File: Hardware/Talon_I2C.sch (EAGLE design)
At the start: 81 parts, among them J1 CONN_TALON_REMOTE, J2 CONN_I2C_LOGGER, J3 CONN_I2C_LOGGER, J4 CONN_I2C_LOGGER, J5 CONN_I2C_LOGGER, Q1 2N7002, Q2 2N7002, Q3 2N7002, Q4 2N7002, Q5 AO3419, Q6 AO3419, Q7 AO3419, Q8 AO3419, U1 SN74HC04, U10 74HC4852, U11 SN74AUP1T157DCK, U12 MCP3421A3, U13 FXMAR2102UMLP, U14 PCA9617WSON, U15 PCA9617WSON, U16 PCA9617WSON, U17 PCA9617WSON, U18 SN74AUP1G08DCK, U19 SN74AUP1G08DCK, U2 CD4044, U20 SN74AUP1G08DCK, U21 SN74AUP1G08DCK, U3 SIP32431TDFN, U4 INA4180A2, U5 MAX9034TSSOP, U6 SN74AC08, U7 24AA02SOT23, U8 MCP23018QFN, U9 PCA9536DFN

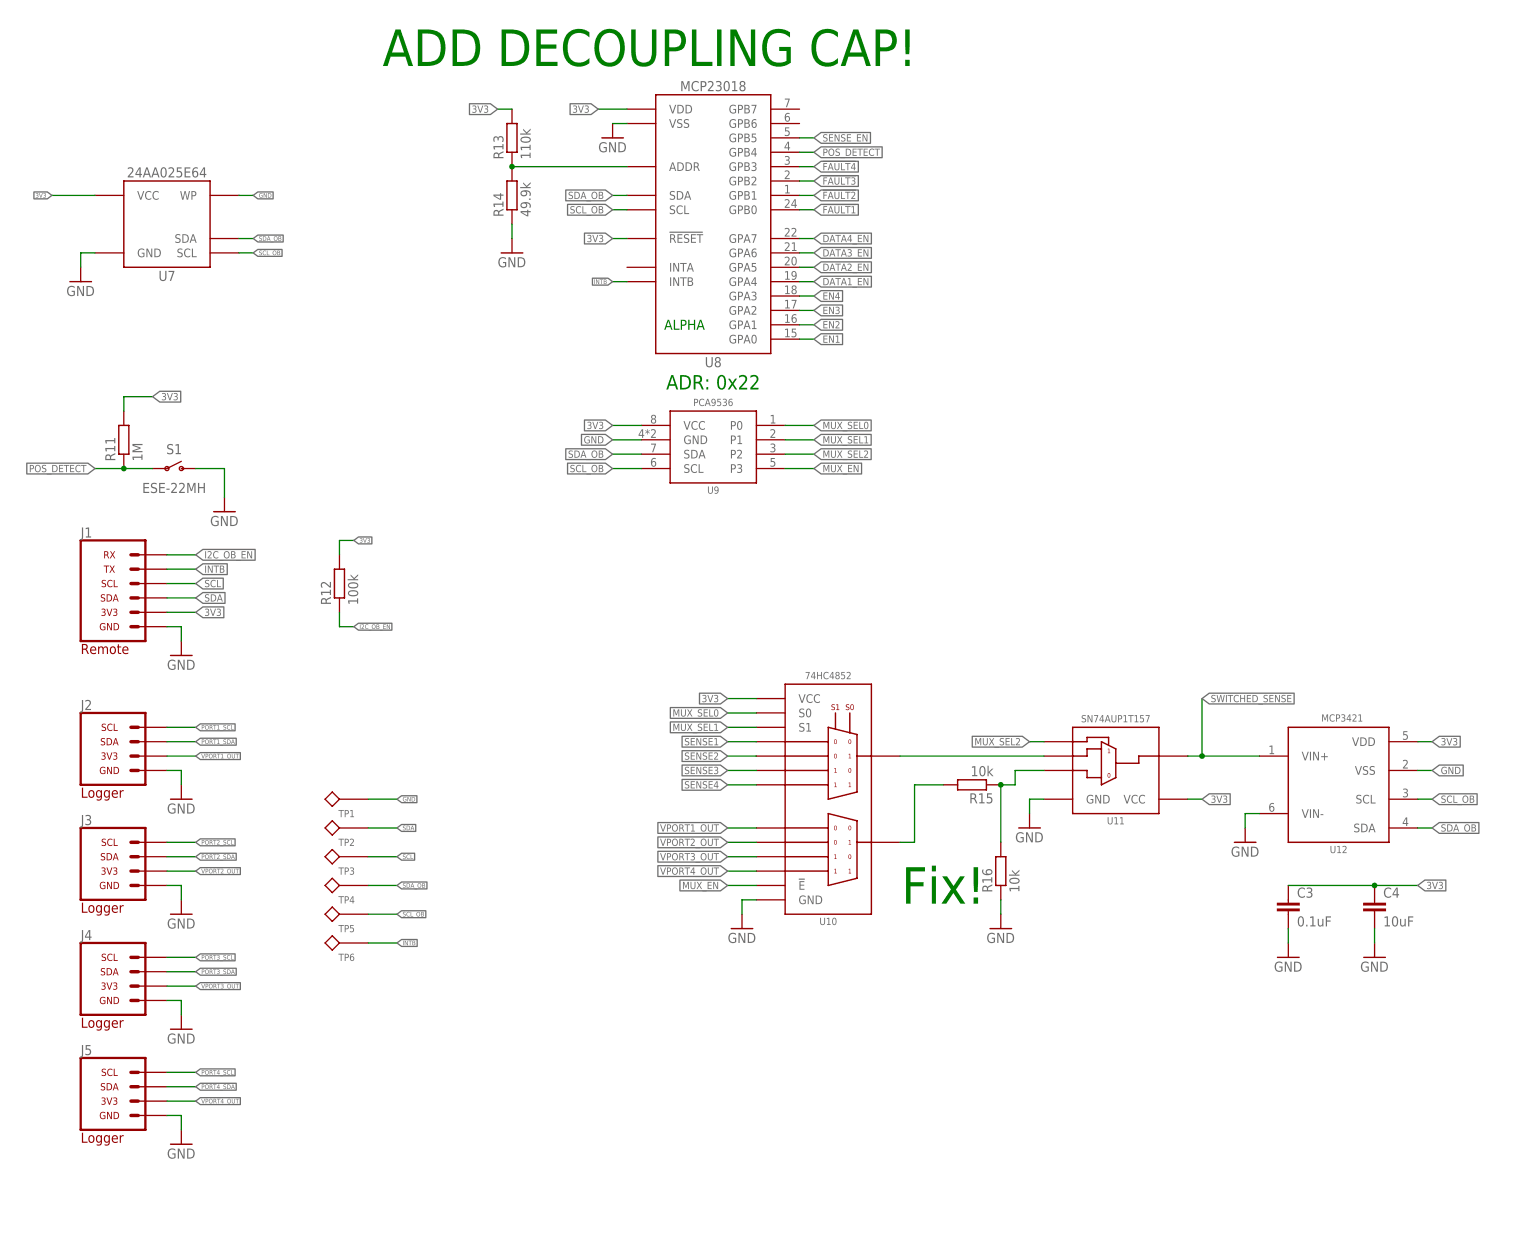
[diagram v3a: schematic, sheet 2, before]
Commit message: Updates for v1.0, sent to fab
Made fixes for v1.0:
- Fixed bypass control
- Added filter lines (clitch protection) to sense lines
- Flipped Talon connector port pinout
- Moved MUX (U9/U10) to prevent soldering issues 
- Moved U6 to prevent bumping
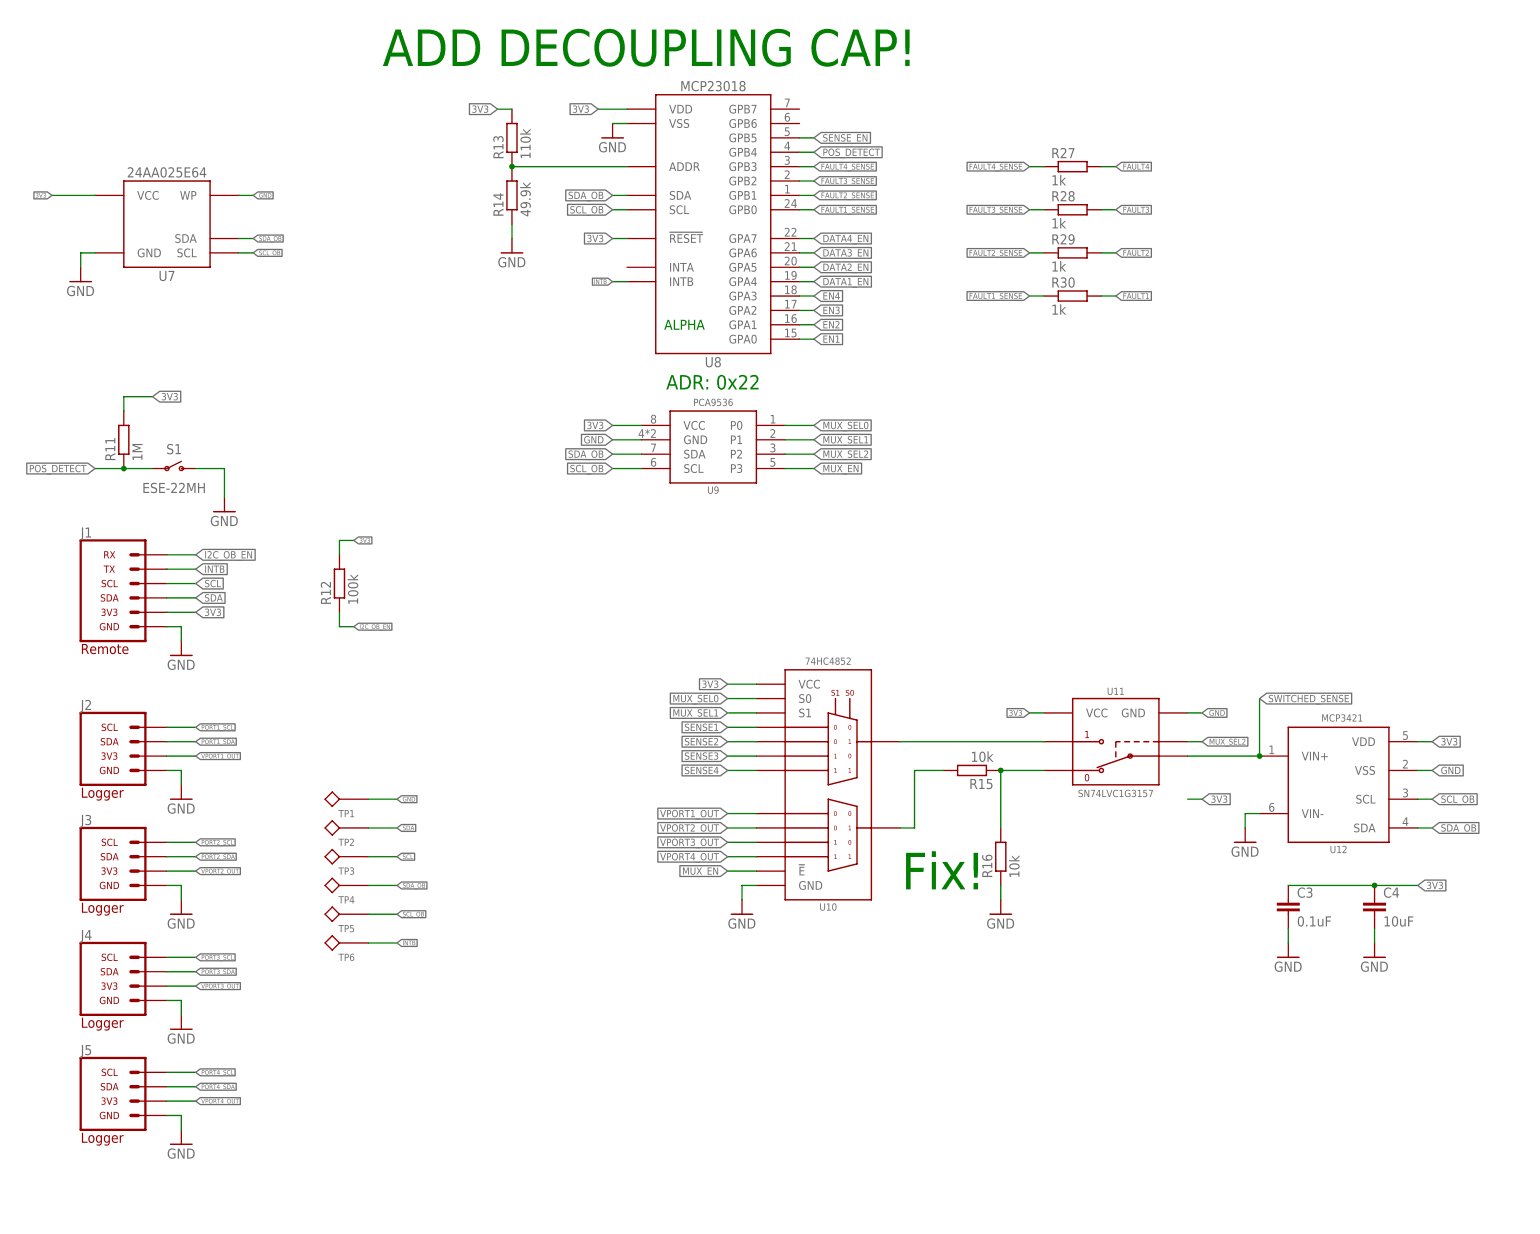
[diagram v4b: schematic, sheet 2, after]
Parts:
- added C14, C15, C16, C17: 0.1uF, bschulz_passives:C-EU0.1UFC0402
- added R27, R28, R29, R30, R31, R32, R33, R34: 1k, bschulz_passives:R-EU_1KR0402
- U11: value SN74AUP1T157DCK -> SN74LVC1G3157SC70; device bschulz:SN74AUP1T157DCK -> bschulz:SN74LVC1G3157SC70
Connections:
- new net FAULT1_SENSE: R30.1, U8.GPB0
- new net FAULT2_SENSE: R29.1, U8.GPB1
- new net FAULT3_SENSE: R28.1, U8.GPB2
- new net FAULT4_SENSE: R27.1, U8.GPB3
- new net SENSE1_FILT: C14.1, R31.2, U5.INA-
- new net SENSE2_FILT: C15.1, R32.2, U5.INB-
- new net SENSE3_FILT: C16.1, R33.2, U5.INC-
- new net SENSE4_FILT: C17.1, R34.2, U5.IND-
- net !FAULT1: now also U1.Y4, U6.B4; no longer U1.A4, U2.Q2, U8.GPB0
- net !FAULT2: now also U1.Y2, U6.B1; no longer U1.A2, U2.Q1, U8.GPB1
- net !FAULT3: now also U1.Y3, U6.B3; no longer U1.A3, U2.Q3, U8.GPB2
- net !FAULT4: now also U1.Y1, U6.B2; no longer U1.A1, U2.Q4, U8.GPB3
- net 3V3: no longer U2.EN
- net FAULT1: now also R30.2, U1.A4, U2.Q2; no longer U1.Y4, U6.B4
- net FAULT2: now also R29.2, U1.A2, U2.Q1; no longer U1.Y2, U6.B1
- net FAULT3: now also R28.2, U1.A3, U2.Q3; no longer U1.Y3, U6.B3
- net FAULT4: now also R27.2, U1.A1, U2.Q4; no longer U1.Y1, U6.B2
- net GND: now also C14.2, C15.2, C16.2, C17.2
- net MUX_SEL2: now also U11.S; no longer U11.C
- net N$38: now also U11.B2; no longer U11.A
- net N$6: now also U11.B1; no longer U11.B
- net SENSE1: now also R31.1; no longer U5.INA-
- net SENSE2: now also R32.1; no longer U5.INB-
- net SENSE3: now also R33.1; no longer U5.INC-
- net SENSE4: now also R34.1; no longer U5.IND-
- net SENSE_EN: now also U2.EN
- net SWITCHED_SENSE: now also U11.A; no longer U11.Y
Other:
- moved on the sheet: R15, R16, U10

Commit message: Part number updates
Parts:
- C14, C15, C16, C17: value 0.1uF -> DNP; DIGIKEY (none) -> DNP; MF (none) -> N/A; MPN (none) -> DNP
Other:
- note added: "ADR: 0x41"
- note added: "ADR: 0x50/0x30"
- note added: "ADR: 0x6B"
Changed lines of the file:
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@@
 <part name="R30" library="bschulz_passives" deviceset="R-EU_" device="R0402" technology="1K" value="1k"/>
 <part name="R31" library="bschulz_passives" deviceset="R-EU_" device="R0402" technology="1K" value="1k"/>
-<part name="C14" library="bschulz_passives" deviceset="C-EU" device="C0402" technology="0.1UF" value="0.1uF"/>
+<part name="C14" library="bschulz_passives" deviceset="C-EU" device="C0402" technology="0.1UF" value="DNP">
+<attribute name="DIGIKEY" value="DNP"/>
+<attribute name="MF" value="N/A"/>
+<attribute name="MPN" value="DNP"/>
+</part>
 <part name="GND2" library="supply1" library_urn="urn:adsk.eagle:library:371" deviceset="GND" device=""/>
 <part name="R32" library="bschulz_passives" deviceset="R-EU_" device="R0402" technology="1K" value="1k"/>
-<part name="C15" library="bschulz_passives" deviceset="C-EU" device="C0402" technology="0.1UF" value="0.1uF"/>
+<part name="C15" library="bschulz_passives" deviceset="C-EU" device="C0402" technology="0.1UF" value="DNP">
+<attribute name="DIGIKEY" value="DNP"/>
+<attribute name="MF" value="N/A"/>
+<attribute name="MPN" value="DNP"/>
+</part>
 <part name="GND3" library="supply1" library_urn="urn:adsk.eagle:library:371" deviceset="GND" device=""/>
 <part name="R33" library="bschulz_passives" deviceset="R-EU_" device="R0402" technology="1K" value="1k"/>
-<part name="C16" library="bschulz_passives" deviceset="C-EU" device="C0402" technology="0.1UF" value="0.1uF"/>
+<part name="C16" library="bschulz_passives" deviceset="C-EU" device="C0402" technology="0.1UF" value="DNP">
+<attribute name="DIGIKEY" value="DNP"/>
+<attribute name="MF" value="N/A"/>
+<attribute name="MPN" value="DNP"/>
+</part>
 <part name="GND7" library="supply1" library_urn="urn:adsk.eagle:library:371" deviceset="GND" device=""/>
 <part name="R34" library="bschulz_passives" deviceset="R-EU_" device="R0402" technology="1K" value="1k"/>
-<part name="C17" library="bschulz_passives" deviceset="C-EU" device="C0402" technology="0.1UF" value="0.1uF"/>
+<part name="C17" library="bschulz_passives" deviceset="C-EU" device="C0402" technology="0.1UF" value="DNP">
+<attribute name="DIGIKEY" value="DNP"/>
+<attribute name="MF" value="N/A"/>
+<attribute name="MPN" value="DNP"/>
+</part>
 <part name="GND10" library="supply1" library_urn="urn:adsk.eagle:library:371" deviceset="GND" device=""/>
 <part name="U11" library="bschulz" deviceset="SN74LVC1G3157" device="SC70"/>
@@
 <text x="170.18" y="60.96" size="6.4516" layer="91" align="center">Fix! </text>
 <text x="129.54" y="147.32" size="2.54" layer="91" align="center">ADR: 0x22</text>
+<text x="231.14" y="60.96" size="2.54" layer="91">ADR: 0x6B</text>
+<text x="25.4" y="160.02" size="2.54" layer="91">ADR: 0x50/0x30</text>
+<text x="121.92" y="121.92" size="2.54" layer="91">ADR: 0x41</text>
 </plain>
 <instances>

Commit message: Updated EEPROM part
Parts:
- U7: value 24AA02SOT23 -> AT24MAC602SOT23; device bschulz:24AA02SOT23 -> bschulz:AT24MAC602SOT23
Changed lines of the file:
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@@
 <part name="J5" library="GEMS_Plugs" deviceset="CONN_I2C_LOGGER" device=""/>
 <part name="GND40" library="supply1" library_urn="urn:adsk.eagle:library:371" deviceset="GND" device=""/>
-<part name="U7" library="bschulz" deviceset="24AA02" device="SOT23"/>
+<part name="U7" library="bschulz" deviceset="AT24MAC*02" device="SOT23" technology="6" value="AT24MAC602SOT23"/>
 <part name="GND56" library="supply1" library_urn="urn:adsk.eagle:library:371" deviceset="GND" device=""/>
 <part name="R16" library="bschulz_passives" deviceset="R-EU_" device="R0402" technology="10K" value="10k"/>
